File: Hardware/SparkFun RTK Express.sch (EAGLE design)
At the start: 105 parts, among them J13 Internal, J17 Qwiic Right Angle, J19 MICRO-SD-PUSH-PUSH-EXT-PIN, J3 USB Female Type C Connector, J4 External, J5 USB Female Type C Connector, Q1 SIL2308-TP, Q2 MBT3904DW1T1, U1 74HC4052D, U10 MCP73833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

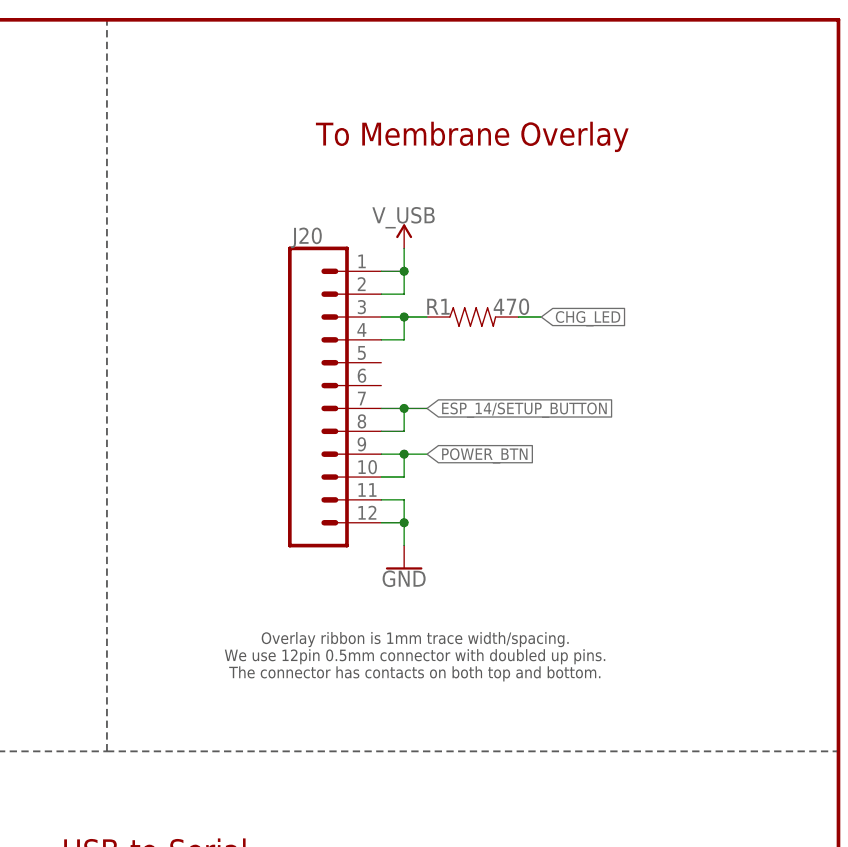
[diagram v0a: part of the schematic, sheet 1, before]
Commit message: LIF overlay connector, accel plane removal, full ESP32 FP.
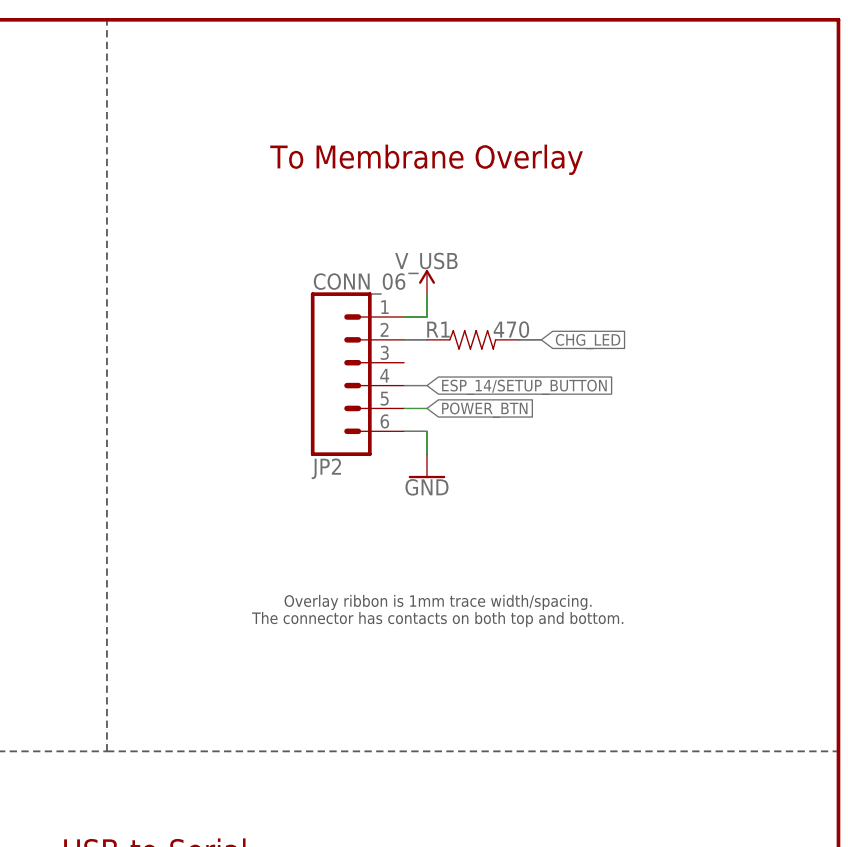
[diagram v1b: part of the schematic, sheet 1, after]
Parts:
- removed J20: (no value), SparkFun-Connectors:CONN_12FPC_12_0.5MM
- added JP2: CONN_06, 1mm Pitch Connector:CONN_06
- renumbered R18 to R6
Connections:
- net CHG_LED_RES: now also JP2.2; no longer J20.3, J20.4
- net ESP_14/SETUP_BUTTON: now also JP2.4; no longer J20.7, J20.8
- net GND: now also JP2.6; no longer J20.11, J20.12
- net POWER_BTN: now also JP2.5; no longer J20.10, J20.9
- net V_USB: now also JP2.1; no longer J20.1, J20.2
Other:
- note added: "Overlay ribbon is 1mm trace width/spacing. The connector has contacts on both top and bottom."
- note removed: "Overlay ribbon is 1mm trace width/spacing. We use 12pin 0.5mm connector with doubled up pins. The connector has contacts on both top and bottom."
- moved on the sheet: R1

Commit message: v15. Fix tCream on LIF connector. Correct CH340 3.3V.
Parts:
- J19: value MICRO-SD-PUSH-PUSH-EXT-PIN -> MICROSD
- JP2: value CONN_06 -> (none); device 1mm Pitch Connector:CONN_06 -> SparkFun-Connectors:CONN_061MM-LIF
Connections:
- removed net N$1: C13.1, C14.1, U6.V3
- net 3.3V: now also C13.1, C14.1, U6.V3, U6.VCC
- net ESP32_!DTR: now also Q2G2.E; no longer Q2Q2.E
- net ESP32_!RTS: now also Q2G1.E; no longer Q2Q1.E
- net ESP32_EN: now also Q2G1.C; no longer Q2Q1.C
- net ESP_0/BOOT: now also Q2G2.C; no longer Q2Q2.C
- net N$24: now also Q2G1.B; no longer Q2Q1.B
- net N$25: now also Q2G2.B; no longer Q2Q2.B
- net V_USB: no longer U6.VCC
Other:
- note added: "7-Bit unshifted I²C address: 0x19"
- note added: "7-Bit unshifted I²C address: 0x36"
- note added: "7-bit unshifted I²C address: 0x42"
- note added: "Part#: ESP32-WROOM-32E-N16"
- note added: "v15"
- note removed: "7-Bit unshifted I2C address: 0x19"
- note removed: "7-bit unshifted I2C address: 0x42"
- note removed: "v12"

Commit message: Add ID panel
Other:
- note added: "Express+: 3.3/10"
- note added: "Express: 10/3.3"
- note added: "Facet LBand: 10/20"
- note added: "Facet: 10/10"
- note added: "IDs:"
- note added: "Surveyor: N/A"
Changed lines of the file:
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@@
 <wire x1="350.52" y1="198.12" x2="350.52" y2="279.4" width="0.2032" layer="97" style="longdash"/>
 <text x="182.88" y="10.16" size="1.778" layer="97" align="center">Part#: ESP32-WROOM-32E-N16</text>
+<text x="274.32" y="114.3" size="1.778" layer="97" align="center-left">IDs:</text>
+<text x="274.32" y="111.76" size="1.778" layer="97" align="center-left">Surveyor: N/A</text>
+<text x="274.32" y="109.22" size="1.778" layer="97" align="center-left">Express: 10/3.3</text>
+<text x="274.32" y="106.68" size="1.778" layer="97" align="center-left">Express+: 3.3/10</text>
+<text x="274.32" y="104.14" size="1.778" layer="97" align="center-left">Facet: 10/10</text>
+<text x="274.32" y="101.6" size="1.778" layer="97" align="center-left">Facet LBand: 10/20</text>
 </plain>
 <instances>
